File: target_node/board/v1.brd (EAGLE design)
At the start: 40.3 x 47 mm, 13 parts, among them IC1 UA741P, U1 L78XXAB/AC/V

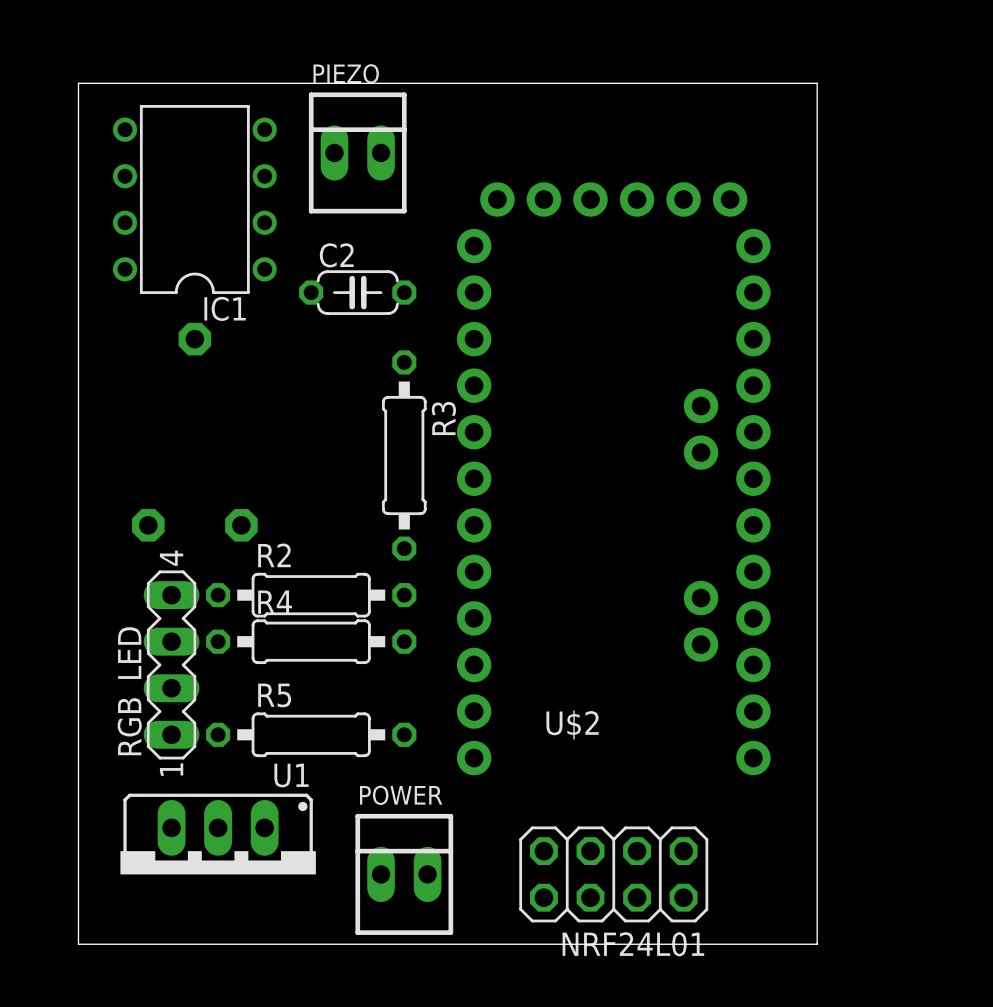
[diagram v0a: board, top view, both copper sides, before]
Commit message: Changed schematic to connect nRF24 board to other digital outputs and make a single layer board
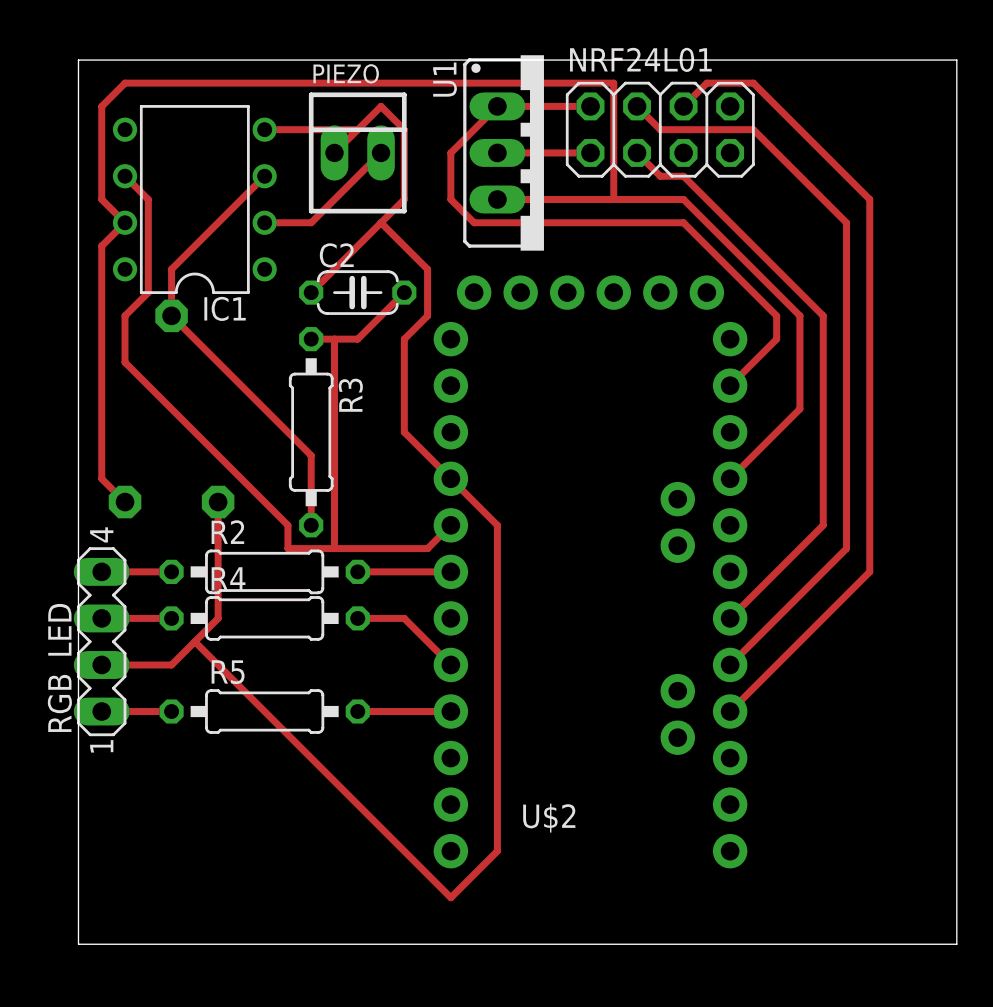
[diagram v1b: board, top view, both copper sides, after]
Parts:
- removed POWER: 22-23-2021, con-molex:22-23-2021
- moved U1 43.2 mm to (24.1, 76.2), turned to 270 degrees
- moved NRF24L01 40.7 mm to (30.5, 77.5), turned to 0 degrees
- moved R3 5.24 mm to (11.4, 61.0)
- moved U$2 5.24 mm to (26.7, 53.3)
- moved RGB_LED 4.02 mm to (0.00, 49.5)
- moved R2 2.84 mm to (8.89, 53.3)
- moved R4 2.84 mm to (8.89, 50.8)
- moved R5 2.84 mm to (8.89, 45.7)
- moved R1 1.80 mm to (3.81, 62.2)
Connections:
- removed net GND: C2.1, IC1.4, NRF24L01.2, PIEZO.1, POWER.2, R1.1, RGB_LED.2, U$2.4, U1.IN
- removed net N$4: NRF24L01.4, U$2.10
- new net N$15: NRF24L01.3, U$2.18
- new net N$17: NRF24L01.2, U$2.23, U1.IN
- new net N$18: C2.1, IC1.4, PIEZO.1, R1.1, RGB_LED.2, U$2.4
- net N$5: now also NRF24L01.4, U$2.17; no longer NRF24L01.3, U$2.11
- net VCC: no longer POWER.1
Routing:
- net N$18: track 0.00 -> 96.5 mm
- net VCC: track 0.00 -> 87.6 mm
- net N$13: track 0.00 -> 52.0 mm
- net N$1: track 0.00 -> 44.4 mm
- net N$5: track 0.00 -> 40.8 mm
- net N$17: track 0.00 -> 36.5 mm
- net N$15: track 0.00 -> 32.5 mm
- net N$16: track 0.00 -> 24.3 mm
- net N$9: track 0.00 -> 7.93 mm
- net N$11: track 0.00 -> 6.13 mm
- net N$14: track 0.00 -> 5.08 mm
- net N$12: track 0.00 -> 5.08 mm
- net N$10: track 0.00 -> 5.08 mm
- net N$8: track 0.00 -> 3.81 mm
- net N$7: track 0.00 -> 3.81 mm
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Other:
- board size 40.3 x 47 mm -> 47.9 x 48.2 mm
